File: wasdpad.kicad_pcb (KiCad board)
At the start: 2 copper layers, 124.8 x 87.3 mm, 22 parts, among them SW1 SW_Push_45deg, SW2 SW_Push_45deg, SW3 SW_Push_45deg, SW4 SW_Push_45deg, SW5 SW_Push_45deg, SW6 SW_Push_45deg, U1 XIAO-RP2040-DIP

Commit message: fix layout + 3d models for mx
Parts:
- moved Brd1 4.76 mm to (96.1, 76.4)
- moved U1 4.76 mm to (86.4, 86.7)
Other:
- board size 124.8 x 87.3 mm -> 64.2 x 61.2 mm
- board text added: "XIAO here!!!"
- board text added: "mr oled"
- board text added: "wow! reverse mounted"
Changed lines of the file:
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@@
 	(footprint "oled:SSD1306-0.91-OLED-4pin-128x32"
 		(layer "F.Cu")
-		(at 96.115 81.115)
+		(at 96.115 76.355)
 		(property "Reference" "Brd1"
 			(at 1.9 5.91 90)
@@
 			(pintype "passive")
 		)
+		(model "${KIPRJMOD}/3d/r3_100.STEP"
+			(offset
+				(xyz -9 -9 10.5)
+			)
+			(scale
+				(xyz 1 1 1)
+			)
+			(rotate
+				(xyz -90 0 0)
+			)
+		)
+		(model "${KIPRJMOD}/3d/MX.STEP"
+			(offset
+				(xyz 7 7.5 6)
+			)
+			(scale
+				(xyz 1 1 1)
+			)
+			(rotate
+				(xyz 90 180 0)
+			)
+		)
 	)
 	(footprint "mx:MX-Solderable-1U"
@@
 			(pintype "passive")
 		)
+		(model "${KIPRJMOD}/3d/r3_100.STEP"
+			(offset
+				(xyz -9 -9 10.5)
+			)
+			(scale
+				(xyz 1 1 1)
+			)
+			(rotate
+				(xyz -90 0 0)
+			)
+		)
+		(model "${KIPRJMOD}/3d/MX.STEP"
+			(offset
+				(xyz 7 7.5 6)
+			)
+			(scale
+				(xyz 1 1 1)
+			)
+			(rotate
+				(xyz 90 180 0)
+			)
+		)
 	)
 	(footprint "mx:MX-Solderable-1U"
@@
 			(pintype "passive")
 		)
+		(model "${KIPRJMOD}/3d/r3_100.STEP"
+			(offset
+				(xyz -9 -9 10.5)
+			)
+			(scale
+				(xyz 1 1 1)
+			)
+			(rotate
+				(xyz -90 0 0)
+			)
+		)
+		(model "${KIPRJMOD}/3d/MX.STEP"
+			(offset
+				(xyz 7 7.5 6)
+			)
+			(scale
+				(xyz 1 1 1)
+			)
+			(rotate
+				(xyz 90 180 0)
+			)
+		)
 	)
 	(footprint "Diode_THT:D_DO-35_SOD27_P7.62mm_Horizontal"
@@
 			(pintype "passive")
 		)
+		(model "${KIPRJMOD}/3d/r3_100.STEP"
+			(offset
+				(xyz -9 -9 10.5)
+			)
+			(scale
+				(xyz 1 1 1)
+			)
+			(rotate
+				(xyz -90 0 0)
+			)
+		)
+		(model "${KIPRJMOD}/3d/MX.STEP"
+			(offset
+				(xyz 7 7.5 6)
+			)
+			(scale
+				(xyz 1 1 1)
+			)
+			(rotate
+				(xyz 90 180 0)
+			)
+		)
 	)
 	(footprint "Diode_THT:D_DO-35_SOD27_P7.62mm_Horizontal"
@@
 			(pintype "passive")
 		)
+		(model "${KIPRJMOD}/3d/r3_100.STEP"
+			(offset
+				(xyz -9 -9 10.5)
+			)
+			(scale
+				(xyz 1 1 1)
+			)
+			(rotate
+				(xyz -90 0 0)
+			)
+		)
+		(model "${KIPRJMOD}/3d/MX.STEP"
+			(offset
+				(xyz 7 7.5 6)
+			)
+			(scale
+				(xyz 1 1 1)
+			)
+			(rotate
+				(xyz 90 180 0)
+			)
+		)
 	)
 	(footprint "mx:MX-Solderable-1U"
@@
 			(pintype "passive")
 		)
+		(model "${KIPRJMOD}/3d/r3_100.STEP"
+			(offset
+				(xyz -9 -9 10.5)
+			)
+			(scale
+				(xyz 1 1 1)
+			)
+			(rotate
+				(xyz -90 0 0)
+			)
+		)
+		(model "${KIPRJMOD}/3d/MX.STEP"
+			(offset
+				(xyz 7 7.5 6)
+			)
+			(scale
+				(xyz 1 1 1)
+			)
+			(rotate
+				(xyz 90 180 0)
+			)
+		)
 	)
 	(footprint "Diode_THT:D_DO-35_SOD27_P7.62mm_Horizontal"
@@
 	(footprint "xiao:XIAO-RP2040-DIP"
 		(layer "F.Cu")
-		(at 86.38 91.46)
+		(at 86.38 86.7)
 		(property "Reference" "U1"
 			(at -8.5 -12 0)
@@
 	)
 	(gr_rect
-		(start 68.75 57.84)
-		(end 193.5 145.15)
+		(start 73.35 76.1)
+		(end 137.55 137.25)
 		(stroke
 			(width 0.05)
@@
 		(layer "Edge.Cuts")
 	)
+	(gr_text "wow! reverse mounted"
+		(at 114.4 115.2 -0)
+		(layer "B.SilkS")
+		(effects
+			(font
+				(size 1 1)
+				(thickness 0.15)
+			)
+			(justify left bottom mirror)
+		)
+	)
+	(gr_text "XIAO here!!!"
+		(at 81.9 89.9 0)
+		(layer "F.SilkS")
+		(effects
+			(font
+				(size 1 1)
+				(thickness 0.15)
+			)
+			(justify left bottom)
+		)
+	)
+	(gr_text "mr oled"
+		(at 112.4 90 0)
+		(layer "F.SilkS")
+		(effects
+			(font
+				(size 1 1)
+				(thickness 0.15)
+			)
+			(justify left bottom)
+		)
+	)
 )

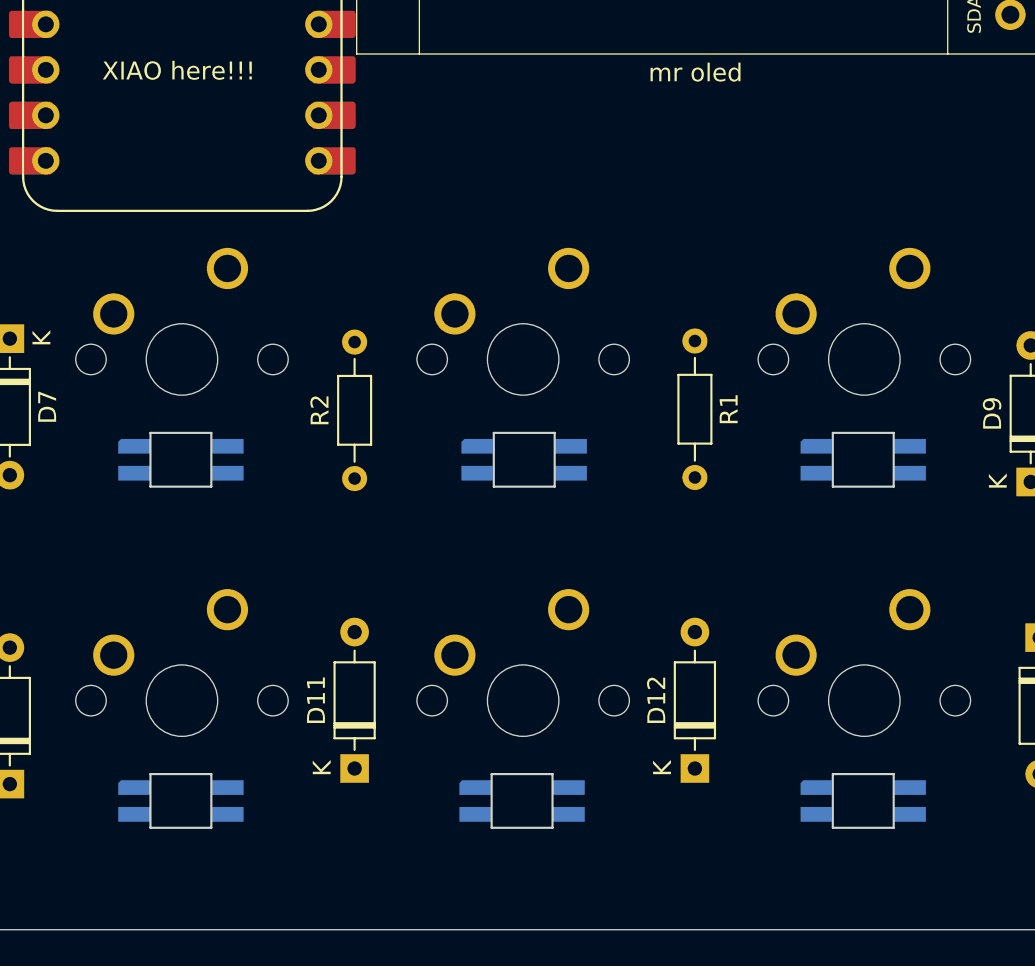
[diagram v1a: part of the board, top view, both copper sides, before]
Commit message: extra neopixels
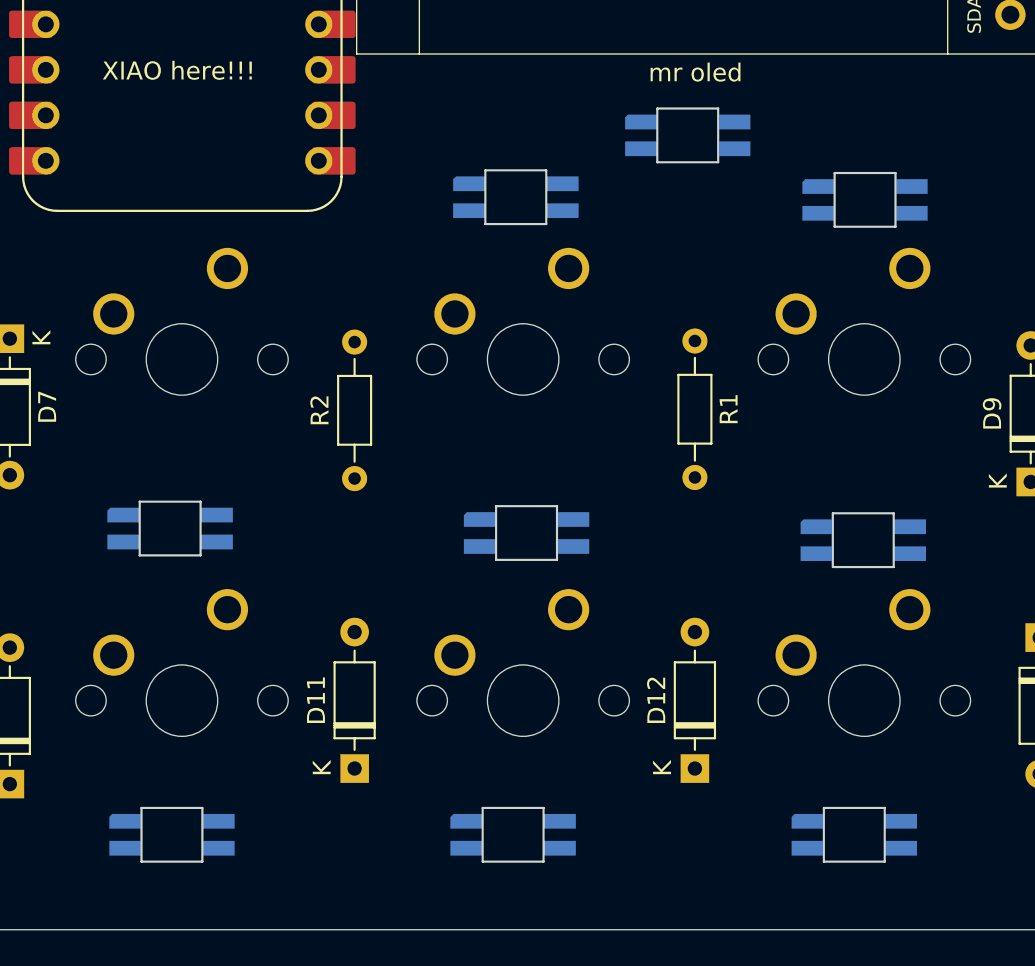
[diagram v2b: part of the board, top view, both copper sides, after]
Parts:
- added D13: SK6812MINI, cyao:SK6812MINI-E, B.Cu at (105.0, 96.3)
- added D14: SK6812MINI, cyao:SK6812MINI-E, B.Cu at (124.5, 96.5)
- added D15: SK6812MINI, cyao:SK6812MINI-E, B.Cu at (114.6, 92.9)
- moved D6 4.49 mm to (124.4, 115.5)
- moved D2 4.09 mm to (105.6, 115.1)
- moved D1 3.89 mm to (85.7, 114.8)
- moved D3 1.96 mm to (123.9, 131.9)
- moved D4 1.96 mm to (104.8, 131.9)
- moved D5 1.96 mm to (85.8, 131.9)
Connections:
- D6 pad 1: unconnected-(D6-DOUT-Pad1) -> Net-(D13-DIN)

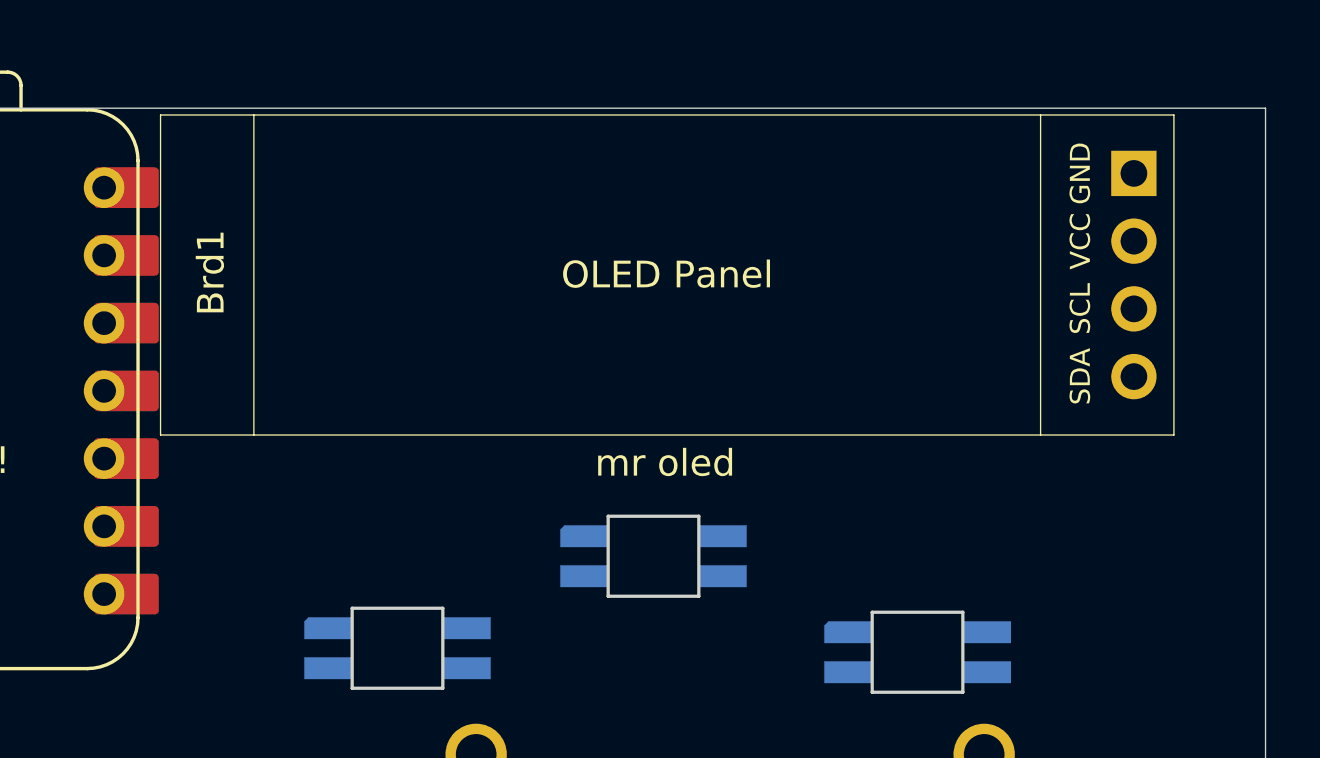
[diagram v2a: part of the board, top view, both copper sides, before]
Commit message: add remaining 3d models
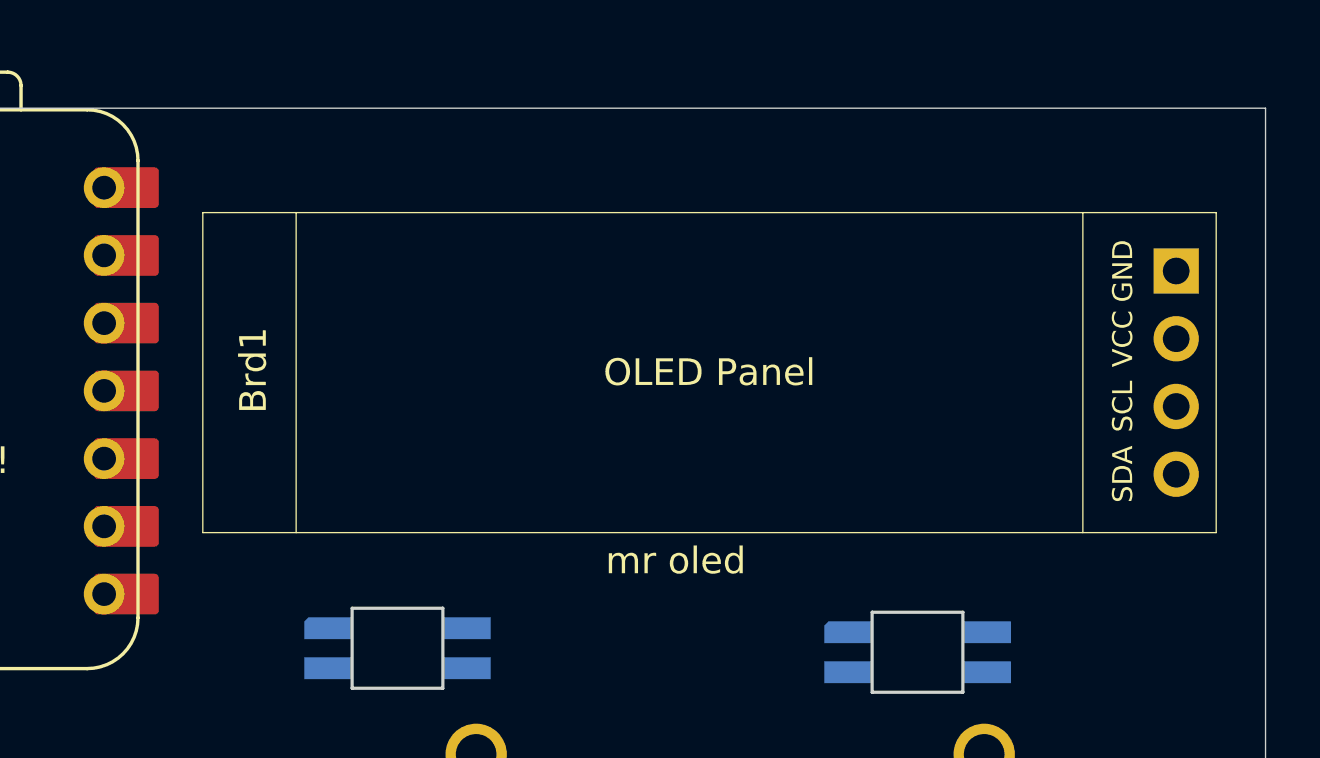
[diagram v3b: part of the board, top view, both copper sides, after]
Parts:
- removed D15: SK6812MINI, cyao:SK6812MINI-E
- moved Brd1 3.99 mm to (97.7, 80.0)
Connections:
- D13 pad 3: Net-(D13-DIN) -> unconnected-(D13-DIN-Pad3)
- D14 pad 1: Net-(D14-DOUT) -> unconnected-(D14-DOUT-Pad1)
- D6 pad 1: Net-(D13-DIN) -> unconnected-(D6-DOUT-Pad1)

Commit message: fix drc issues
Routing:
- net +5V: track 0.00 -> 295.3 mm, vias 0 -> 10
- net SDA: track 0.00 -> 105.6 mm
- net Row 0: track 0.00 -> 104.5 mm, vias 0 -> 1
- net Col 2: track 0.00 -> 84.3 mm, vias 0 -> 4
- net SCL: track 0.00 -> 83.1 mm
- net Row 1: track 0.00 -> 75.9 mm, vias 0 -> 1
- net LEDin: track 0.00 -> 68.7 mm
- net Col 1: track 0.00 -> 66.2 mm, vias 0 -> 4
- net Col 0: track 0.00 -> 56.4 mm, vias 0 -> 1
- net Net-(D8-A): track 0.00 -> 55.3 mm
- net +3V3: track 0.00 -> 44.8 mm, vias 0 -> 1
- net Net-(D5-DOUT): track 0.00 -> 40.4 mm, vias 0 -> 2
- net DOUT: track 0.00 -> 32.8 mm, vias 0 -> 2
- net Net-(D4-DOUT): track 0.00 -> 28.0 mm, vias 0 -> 2
- net Net-(D2-DOUT): track 0.00 -> 27.9 mm, vias 0 -> 2
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- added copper zone on B.Cu, net GND
